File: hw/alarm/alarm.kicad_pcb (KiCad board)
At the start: 2 copper layers, 105 x 73 mm, 60 parts, among them IC1 DS3231S#T&R, IC2 TSOP38238, IC3 SHT40-BD1B-R2, IC4 23K256-I_SN, IC5 PEC11S-929K-S0015, J1 4328, J2 SFV24R-4STBE1HLF, Q1 DMG2305UX-7, Q3 Si1308EDL-T1-GE3, U1 RaspberryPi_Pico, U3 2462, U4 AS1115-BSST, U5 TDCR1060M

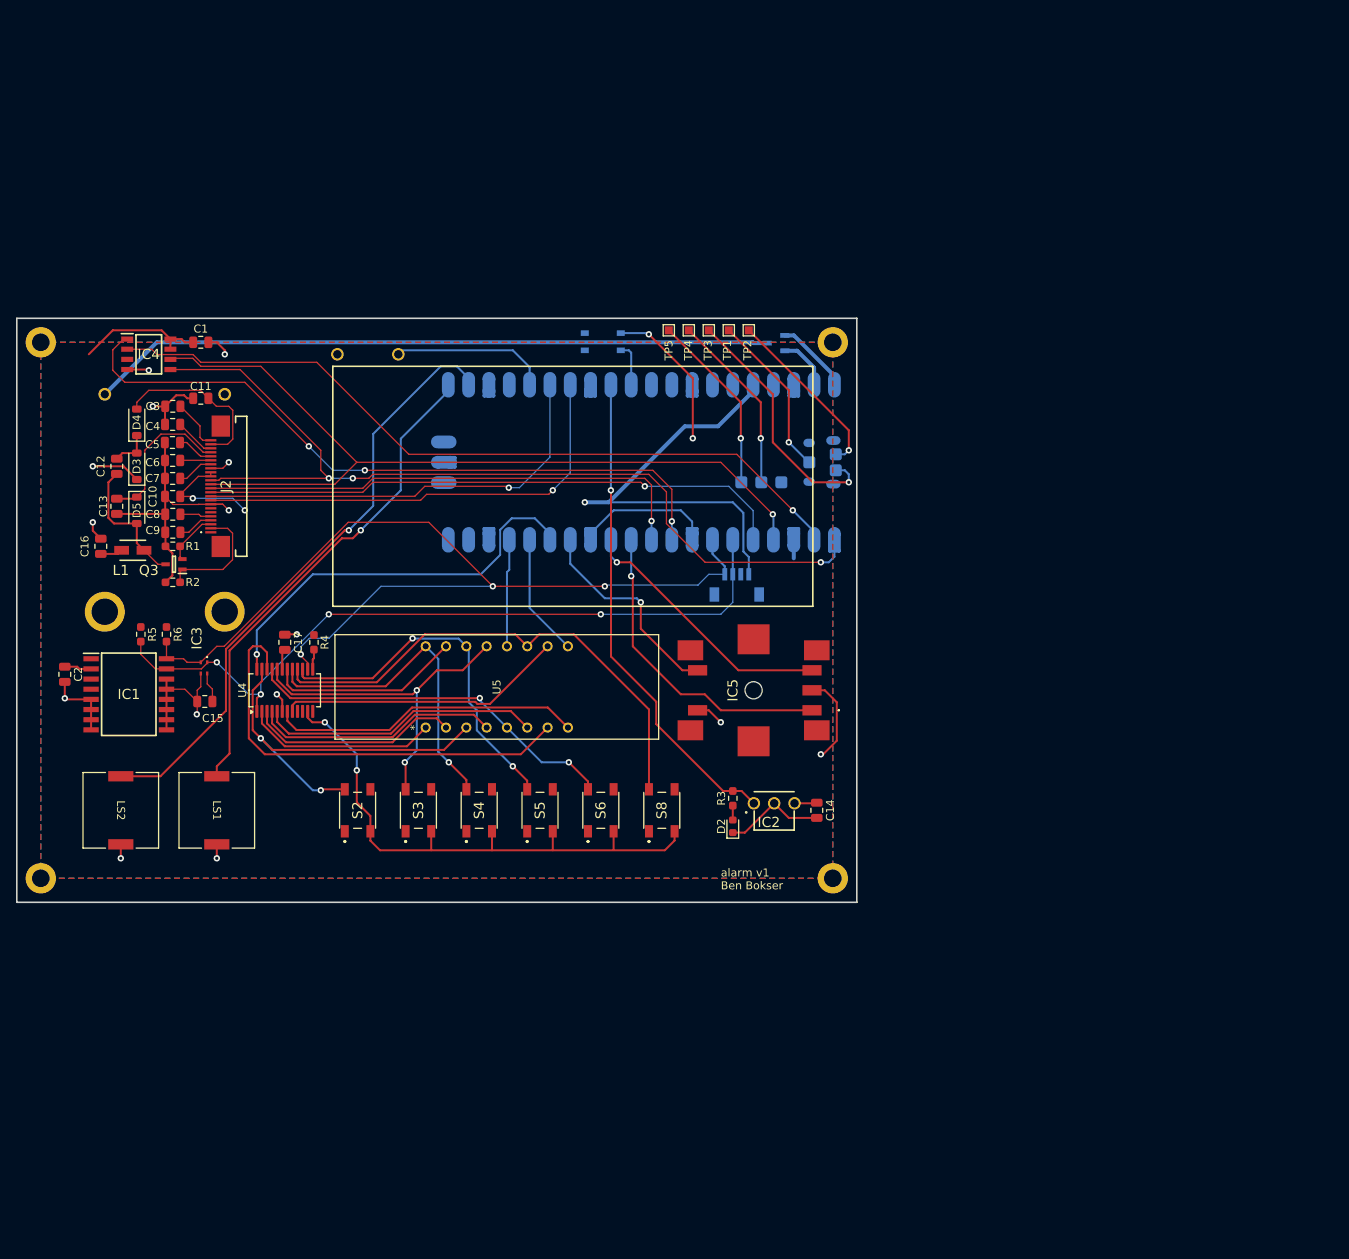
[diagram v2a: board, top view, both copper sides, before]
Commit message: Finish v2 schematic and begin v2 board layout
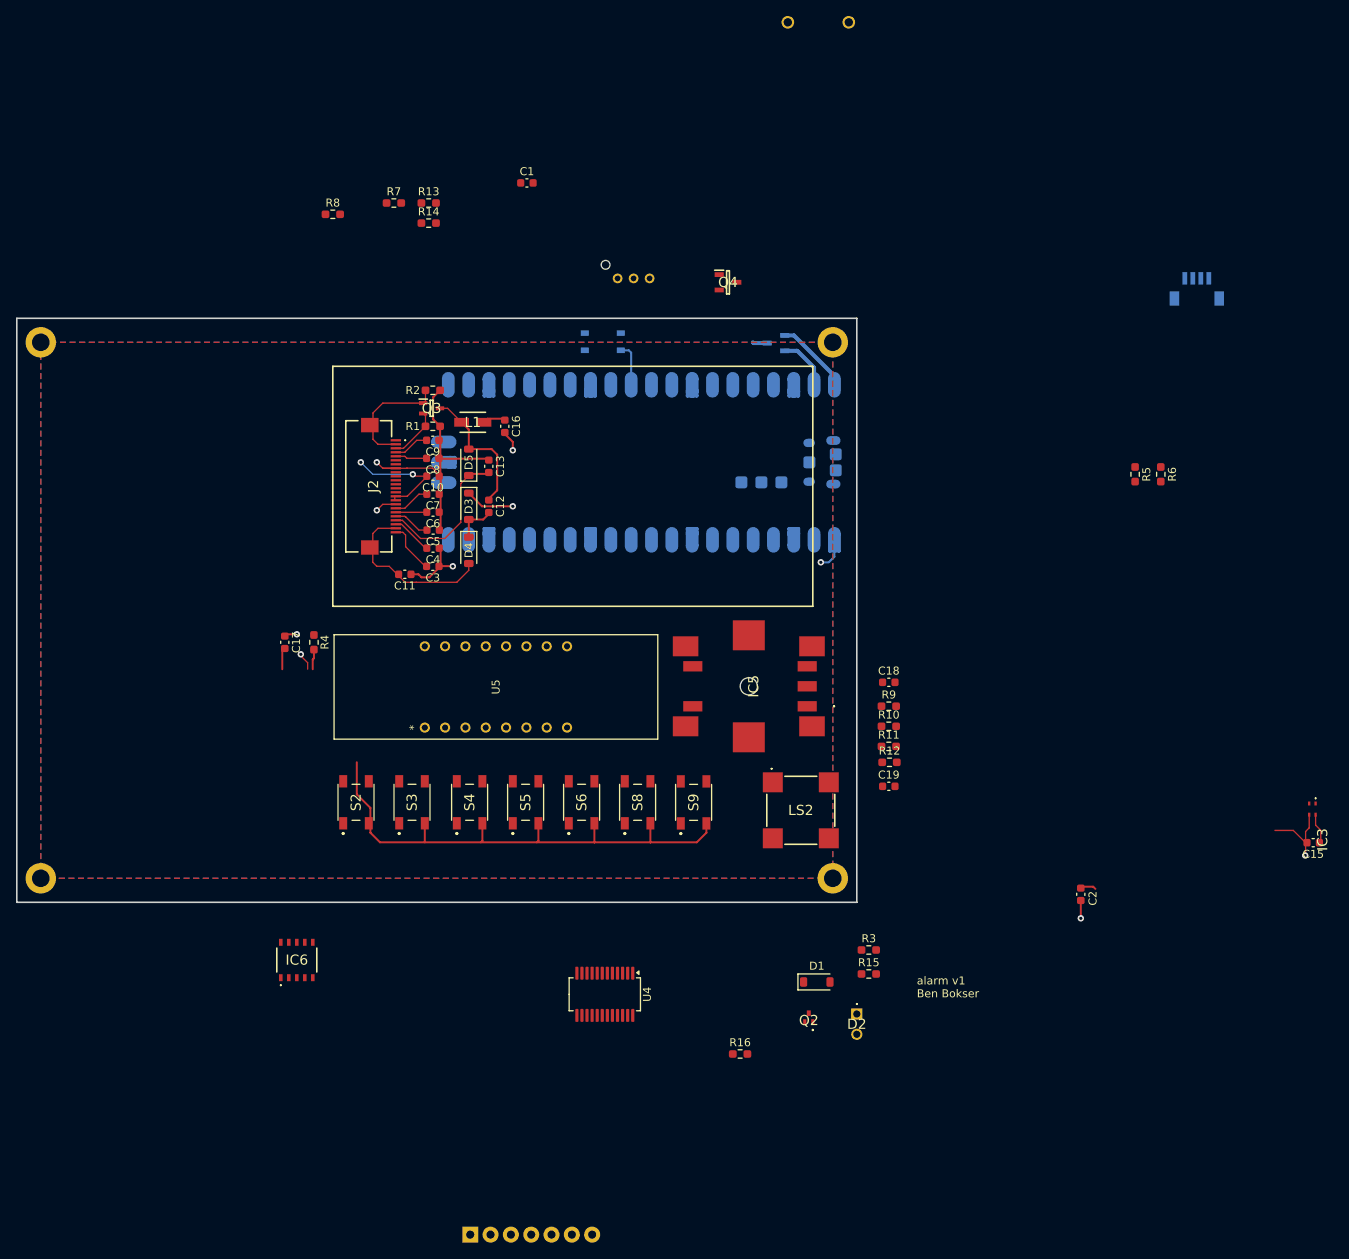
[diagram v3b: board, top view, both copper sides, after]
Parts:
- removed C14: 1uF, Capacitor_SMD:C_0805_2012Metric
- removed IC1: DS3231S#T&R, SamacSys_Parts:SOIC127P1032X265-16N
- removed IC2: TSOP38238, SamacSys_Parts:TSOP38238
- removed IC4: 23K256-I_SN, SamacSys_Parts:SOIC127P600X175-8N
- removed LS1: CPT-9019A-SMT-TR, CPT_9019A_SMT_TR:CPT-9019A_CUD
- removed TP1, TP2, TP3, TP4, TP5: TestPoint, TestPoint:TestPoint_Pad_1.0x1.0mm
- removed U3: 2462, SamacSys_Parts:2462
- added A1: ~, RX480E:RX480E, B.Cu at (142.6, 173.5)
- added C18: 1uF, Capacitor_SMD:C_0603_1608Metric, F.Cu at (197.5, 107.0)
- added C19: 1uF, Capacitor_SMD:C_0603_1608Metric, F.Cu at (197.5, 120.0)
- added D1: MBR0530, Diode_SMD:D_SOD-123, F.Cu at (188.5, 144.5)
- added IC6: MAX31328NELB+, SamacSys_Parts:MAX31328NELB, F.Cu at (123.5, 141.7)
- added J3: 975, SamacSys_Parts:975, B.Cu at (163.6, 56.5)
- added Q2: 2SC5585TL, SamacSys_Parts:2SC5585TL, F.Cu at (187.5, 148.9)
- added Q4: DMG2305UX-7, SamacSys_Parts:SOT96P240X115-3N, F.Cu at (177.4, 57.0)
- added R10: 10kΩ, Resistor_SMD:R_0603_1608Metric_Pad0.98x0.95mm_HandSolder, F.Cu at (197.5, 112.5)
- added R11: 10kΩ, Resistor_SMD:R_0603_1608Metric_Pad0.98x0.95mm_HandSolder, F.Cu at (197.5, 115.0)
- added R12: 10kΩ, Resistor_SMD:R_0603_1608Metric_Pad0.98x0.95mm_HandSolder, F.Cu at (197.6, 117.0)
- added R13: 130Ω, Resistor_SMD:R_0603_1608Metric_Pad0.98x0.95mm_HandSolder, F.Cu at (140.0, 47.1)
- added R14: 10kΩ, Resistor_SMD:R_0603_1608Metric_Pad0.98x0.95mm_HandSolder, F.Cu at (140.0, 49.6)
- added R15: 47Ω, Resistor_SMD:R_0603_1608Metric_Pad0.98x0.95mm_HandSolder, F.Cu at (195.0, 143.5)
- added R16: 180Ω, Resistor_SMD:R_0603_1608Metric_Pad0.98x0.95mm_HandSolder, F.Cu at (178.9, 153.5)
- added R7: 130Ω, Resistor_SMD:R_0603_1608Metric_Pad0.98x0.95mm_HandSolder, F.Cu at (135.6, 47.1)
- added R8: 10kΩ, Resistor_SMD:R_0603_1608Metric_Pad0.98x0.95mm_HandSolder, F.Cu at (128.0, 48.5)
- added R9: 10kΩ, Resistor_SMD:R_0603_1608Metric_Pad0.98x0.95mm_HandSolder, F.Cu at (197.5, 110.0)
- added S9: PTS647SM70SMTR2LFS, SamacSys_Parts:PTS647SM38SMTR2LFS, F.Cu at (173.1, 122.0)
- C1: value 1uF -> 4.7uF; footprint Capacitor_SMD:C_0805_2012Metric -> Capacitor_SMD:C_0603_1608Metric
- C10, C11, C12, C13, C15, C16, C17, C2, C3, C4, C5, C6, C7, C8, C9: footprint Capacitor_SMD:C_0805_2012Metric -> Capacitor_SMD:C_0603_1608Metric
- D2: footprint LED_SMD:LED_0603_1608Metric -> SamacSys_Parts:WP710A10LID
- J2: value SFV24R-4STBE1HLF -> FFC2B35-24-T; footprint SamacSys_Parts:SFV24R4STBE1HLF -> SamacSys_Parts:FFC2B3524T
- LS2: value CPT-9019A-SMT-TR -> CSS-I4B20-SMT-TR; footprint CPT_9019A_SMT_TR:CPT-9019A_CUD -> SamacSys_Parts:CSSI4B20SMTTR
- R3: value 267Ω -> 1kΩ
- R4: value 10kΩ -> 13.9kΩ
- moved C15 139.7 mm to (250.6, 127.0)
- moved IC3 139.7 mm to (250.4, 122.8)
- moved C2 129.9 mm to (221.5, 133.5)
- moved R6 125.9 mm to (231.5, 81.0)
- moved R5 125.9 mm to (228.3, 81.0)
- moved LS2 85.0 mm to (186.5, 123.0), turned to 0 degrees
- moved S7 70.0 mm to (184.9, 24.5)
- moved J1 68.4 mm to (236.0, 58.3)
- moved U4 55.2 mm to (162.0, 146.0), turned to -90 degrees
- moved C16 52.7 mm to (149.5, 75.0), turned to -90 degrees
- moved C12 46.8 mm to (147.5, 85.0), turned to -90 degrees
- moved C13 46.8 mm to (147.5, 80.0), turned to -90 degrees
- moved L1 45.4 mm to (145.5, 74.5), turned to 180 degrees
- moved C1 45.4 mm to (152.3, 44.6)
- moved D4 44.5 mm to (145.0, 90.5), turned to -90 degrees
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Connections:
- C1 pad 1: +3.3V -> GND
- C1 pad 2: GND -> +3.3V
- IC3 pad 3: GND -> +3.3V
- IC3 pad 4: +3.3V -> GND
- IC5 pad A1: /Enc_A1 -> Net-(IC5-CCW)
- IC5 pad B1: /Enc_B1 -> Net-(IC5-CW)
- IC5 pad D1: GND -> /Enc_D
- IC5 pad E1: /Enc_Switch -> /Enc_E
- J1 pad 1: /SCL -> GND
- J1 pad 2: /SDA -> +3.3V
- J1 pad 3: GND -> /SDA
- J1 pad 4: +3.3V -> /SCL
- LS2 pad 1: Net-(U1-GPIO17) -> +3.3V
- LS2 pad 2: GND -> Net-(D1-A)
- R3 pad 1: Net-(D2-A) -> /RF_key
- R3 pad 2: Net-(IC2-OUT) -> +3.3V
- S2 pad 3: /KEYA -> /Enc_D
- S3 pad 3: /KEYA -> /Enc_D
- S4 pad 3: /KEYA -> /Enc_D
- S5 pad 3: /KEYA -> /Enc_D
- S6 pad 3: /KEYA -> /Enc_D
- S8 pad 3: /KEYA -> /Enc_D
- U1 pad 1: /MOSI -> unconnected-(U1-GPIO0-Pad1)
- U1 pad 14: /Enc_Switch -> Net-(S7-NO)
- U1 pad 19: unconnected-(U1-GPIO14-Pad19) -> /RTC_INT
- U1 pad 2: /MISO -> unconnected-(U1-GPIO1-Pad2)
- U1 pad 20: unconnected-(U1-GPIO15-Pad20) -> /Buzzer
- U1 pad 21: Net-(U1-GPIO16) -> /EinkRESET
- U1 pad 22: Net-(U1-GPIO17) -> /EinkBUSY
- U1 pad 24: unconnected-(U1-GPIO18-Pad24) -> /SCK
- U1 pad 25: Net-(S7-NO) -> /MOSI
- U1 pad 26: /EinkRESET -> /MISO
- U1 pad 27: /EinkBUSY -> /DC
- U1 pad 29: Net-(IC2-OUT) -> unconnected-(U1-GPIO22-Pad29)
- U1 pad 4: /SCK -> /RF_key
- U1 pad 5: /DC -> /RF1
- U1 pad 9: /SRAMCS -> unconnected-(U1-GPIO6-Pad9)
- U1 pad TP1: Net-(U1-USB_GND) -> unconnected-(U1-USB_GND-PadTP1)
- U1 pad TP2: Net-(U1-USB_DM) -> unconnected-(U1-USB_DM-PadTP2)
- U1 pad TP3: Net-(U1-USB_DP) -> unconnected-(U1-USB_DP-PadTP3)
- U1 pad TP5: Net-(U1-LED_OUT) -> unconnected-(U1-LED_OUT-PadTP5)
- U1 pad TP6: Net-(U1-~{BOOTSEL}) -> unconnected-(U1-~{BOOTSEL}-PadTP6)
- U4 pad 11: /KEYA -> /Enc_D
- U4 pad 22: Net-(U4-SEGDP) -> /Enc_E
- U4 pad 7: Net-(U4-DIG4) -> unconnected-(U4-DIG4-Pad7)
- U4 pad 8: Net-(U4-DIG5) -> unconnected-(U4-DIG5-Pad8)
- U5 pad 10: Net-(U4-DIG5) -> Net-(U5-CC_L3)
- U5 pad 4: Net-(U4-DIG2) -> Net-(U5-CC_L1_L2)
- U5 pad 6: Net-(U4-DIG3) -> Net-(U4-DIG2)
- U5 pad 7: Net-(U4-SEGDP) -> /Enc_E
- U5 pad 8: Net-(U4-DIG4) -> Net-(U4-DIG3)
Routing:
- net /SCL: track 119.4 -> 2.32 mm, vias 3 -> 1
- net /MOSI: track 115.2 -> 0.00 mm, vias 3 -> 0
- net /SCK: track 105.2 -> 0.00 mm, vias 1 -> 0
- net /MISO: track 95.5 -> 0.00 mm, vias 1 -> 0
- net /SDA: track 95.0 -> 0.00 mm, vias 4 -> 0
- net GND: track 157.6 -> 67.3 mm, vias 17 -> 8
- net /SRAMCS: track 86.5 -> 0.00 mm, vias 3 -> 0
- net Net-(Q1-D): track 85.5 -> 1.84 mm
- net Net-(U1-GPIO17): track 76.7 -> 0.00 mm, vias 1 -> 0
- net /DC: track 72.6 -> 0.00 mm, vias 1 -> 0
- net +3.3V: track 97.8 -> 25.2 mm, vias 3 -> 2
- net /KEYA: track 69.9 -> 0.00 mm, vias 2 -> 0
- net /Enc_D: track 0.00 -> 65.7 mm
- net Net-(U4-SEGF): track 63.0 -> 0.00 mm
- net /EinkCS: track 62.0 -> 0.00 mm, vias 1 -> 0
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
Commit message: Continue board layout
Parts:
- Q1, S1: moved to F.Cu
- moved C2 98.9 mm to (129.0, 98.6), turned to 90 degrees
- moved R13 69.2 mm to (146.0, 116.0)
- moved R7 56.1 mm to (156.2, 99.2), turned to 180 degrees
- moved C1 54.0 mm to (142.8, 97.8)
- moved U4 52.1 mm to (148.2, 95.8), turned to 180 degrees
- moved R14 49.0 mm to (138.0, 98.6), turned to -90 degrees
- moved S7 46.9 mm to (147.6, 53.0)
- moved IC6 46.3 mm to (133.5, 96.5)
- moved R15 40.7 mm to (157.0, 158.0), turned to 180 degrees
- moved R3 37.7 mm to (161.8, 158.2)
- moved Q4 36.5 mm to (141.8, 65.2), turned to 180 degrees
- moved REF** 34.0 mm to (125.5, 64.5)
- moved REF** 34.0 mm to (125.5, 131.5)
- moved D2 32.9 mm to (163.8, 162.5)
- moved J3 32.7 mm to (133.2, 68.8), turned to -90 degrees
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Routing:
- net /Enc_D: track 65.7 -> 112.1 mm
- net GND: track 67.3 -> 22.2 mm
- net Net-(U4-DIG0): track 0.00 -> 28.9 mm
- net /Enc_E: track 0.00 -> 22.4 mm
- net /VGL: track 21.1 -> 0.00 mm
- net Net-(U4-DIG3): track 0.00 -> 21.1 mm
- net /VGH: track 18.9 -> 0.00 mm
- net Net-(U4-SEGE): track 0.00 -> 17.9 mm
- net +3.3V: track 25.2 -> 7.62 mm, vias 2 -> 0
- net Net-(U4-DIG2): track 0.00 -> 17.5 mm
- net Net-(D5-A): track 16.9 -> 0.00 mm
- net Net-(U4-SEGD): track 0.00 -> 15.8 mm
- net /GDR: track 14.8 -> 1.72 mm
- net Net-(U4-SEGB): track 0.00 -> 12.4 mm
- net Net-(U4-SEGF): track 0.00 -> 11.7 mm
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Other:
- board size 105 x 73 mm -> 71 x 73 mm
